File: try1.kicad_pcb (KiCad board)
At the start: 2 copper layers, 175.3 x 119.4 mm, 33 parts, among them J10 Archon-connector-modules-Driv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, J11 Archon-connector-modules-Driv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, J2 Archon-connector-modules-Heat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, J21 DB37, J22 DB37, J3 Archon-connector-modules-Driv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, J31 DB9, J4 Archon-connector-modules-LVBi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, J41 CONN_DVI, J5 Archon-connector-modules-ADC, J6 Archon-connector-modules-ADC, J7 Archon-connector-modules-ADC, J8 Archon-connector-modules-ADC, J9 Archon-connector-modules-HVBi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, P1 CONN_02X02

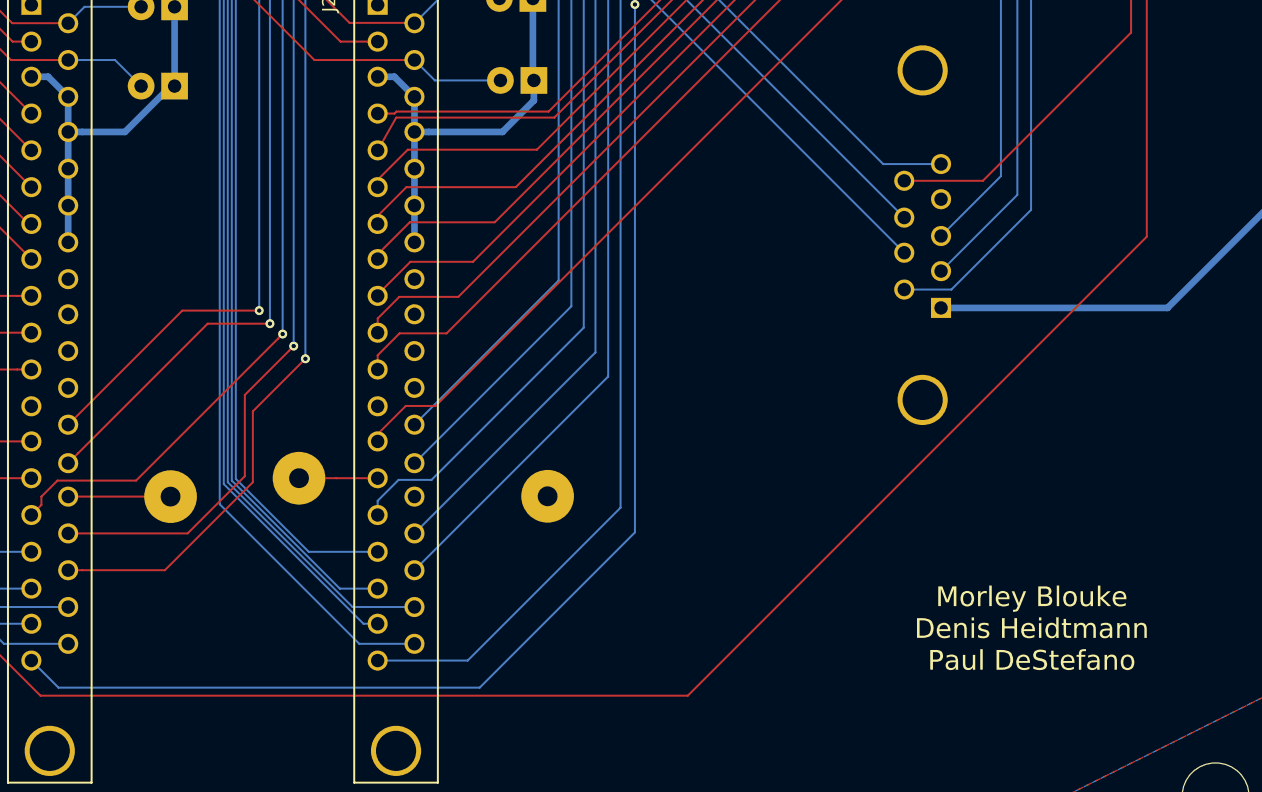
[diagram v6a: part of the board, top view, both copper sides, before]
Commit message: Add Ralf & Erik, Tweak GND Traces
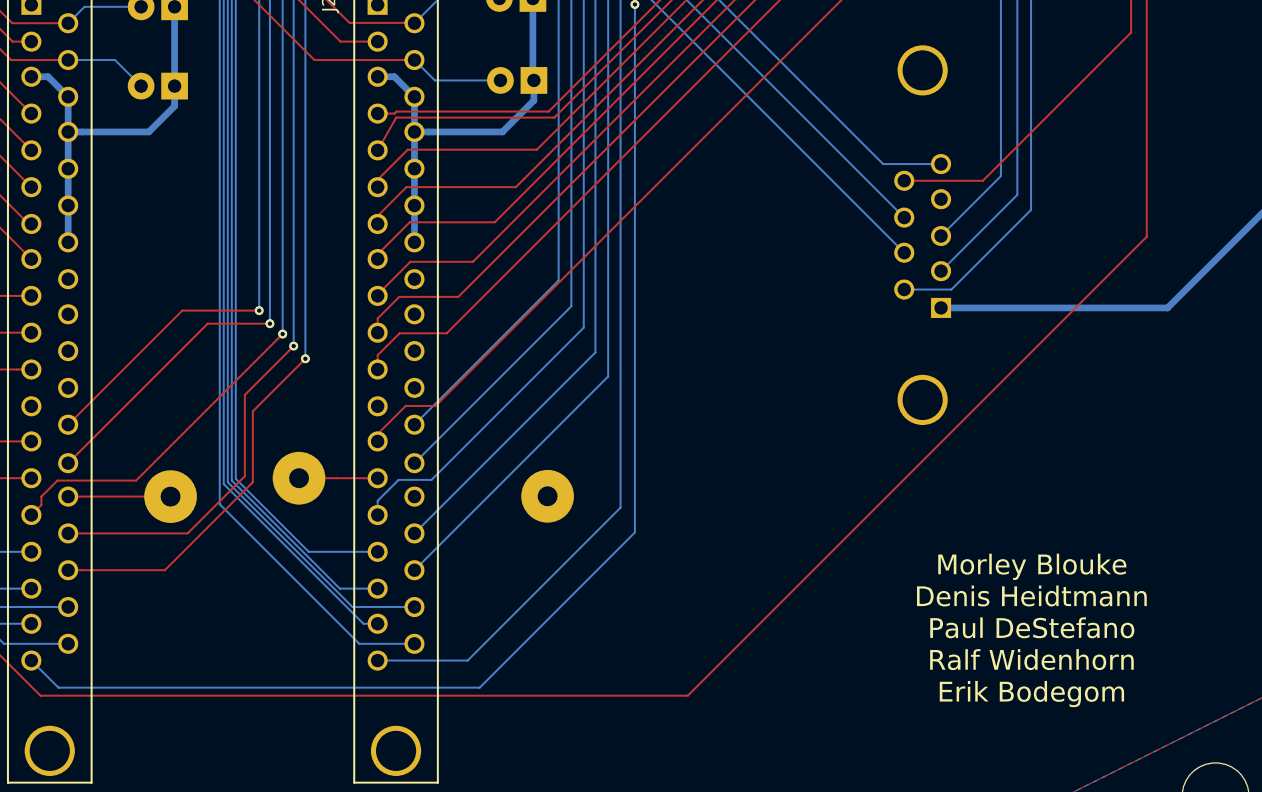
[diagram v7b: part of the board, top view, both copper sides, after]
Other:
- board text added: "Morley Blouke Denis Heidtmann Paul DeStefano Ralf Widenhorn Erik Bodegom"
- board text removed: "Morley Blouke Denis Heidtmann Paul DeStefano"
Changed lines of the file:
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@@
     (pad "" np_thru_hole circle (at -6.6 1.524 90) (size 1.524 1.524) (drill 1.524) (layers *.Cu *.Mask F.SilkS))
   )
-  (gr_text "Morley Blouke\nDenis Heidtmann\nPaul DeStefano" (at 197.6374 122.1486) (layer F.SilkS)
+  (gr_text "Morley Blouke\nDenis Heidtmann\nPaul DeStefano\nRalf Widenhorn\nErik Bodegom" (at 197.6374 122.1486) (layer F.SilkS)
     (effects (font (size 1.5 1.5) (thickness 0.3)))
   )
@@
   (target plus (at 52.07 99.06) (size 5) (width 0.15) (layer Edge.Cuts))
   (target plus (at 52.07 35.56) (size 5) (width 0.15) (layer Edge.Cuts))
+  (segment (start 132.5626 80.9498) (end 132.5626 82.4738) (width 0.508) (layer B.Cu) (net 23))
+  (segment (start 132.5626 82.4738) (end 130.6068 84.4296) (width 0.508) (layer B.Cu) (net 23))
+  (segment (start 130.6068 84.4296) (end 125.56173 84.4296) (width 0.508) (layer B.Cu) (net 23))
+  (segment (start 125.56173 84.4296) (end 124.4841 84.4296) (width 0.508) (layer B.Cu) (net 23))
   (segment (start 150.7744 90.0176) (end 150.7744 92.8116) (width 0.508) (layer B.Cu) (net 23))
   (segment (start 150.7744 87.2236) (end 150.7744 90.0176) (width 0.508) (layer B.Cu) (net 23))
@@
   (segment (start 121.6901 80.2386) (end 122.9601 80.2386) (width 0.508) (layer B.Cu) (net 23))
   (segment (start 122.9601 80.2386) (end 124.4841 81.7626) (width 0.508) (layer B.Cu) (net 23))
-  (segment (start 132.5626 80.9498) (end 132.562599 80.665323) (width 0.508) (layer B.Cu) (net 23))
-  (segment (start 132.562599 80.665323) (end 128.798322 84.4296) (width 0.508) (layer B.Cu) (net 23))
-  (segment (start 128.798322 84.4296) (end 125.56173 84.4296) (width 0.508) (layer B.Cu) (net 23))
-  (segment (start 125.56173 84.4296) (end 124.4841 84.4296) (width 0.508) (layer B.Cu) (net 23))
   (segment (start 124.4841 90.0176) (end 124.4841 92.8116) (width 0.508) (layer B.Cu) (net 23))
   (segment (start 124.4841 90.0176) (end 124.4841 87.2236) (width 0.508) (layer B.Cu) (net 23))

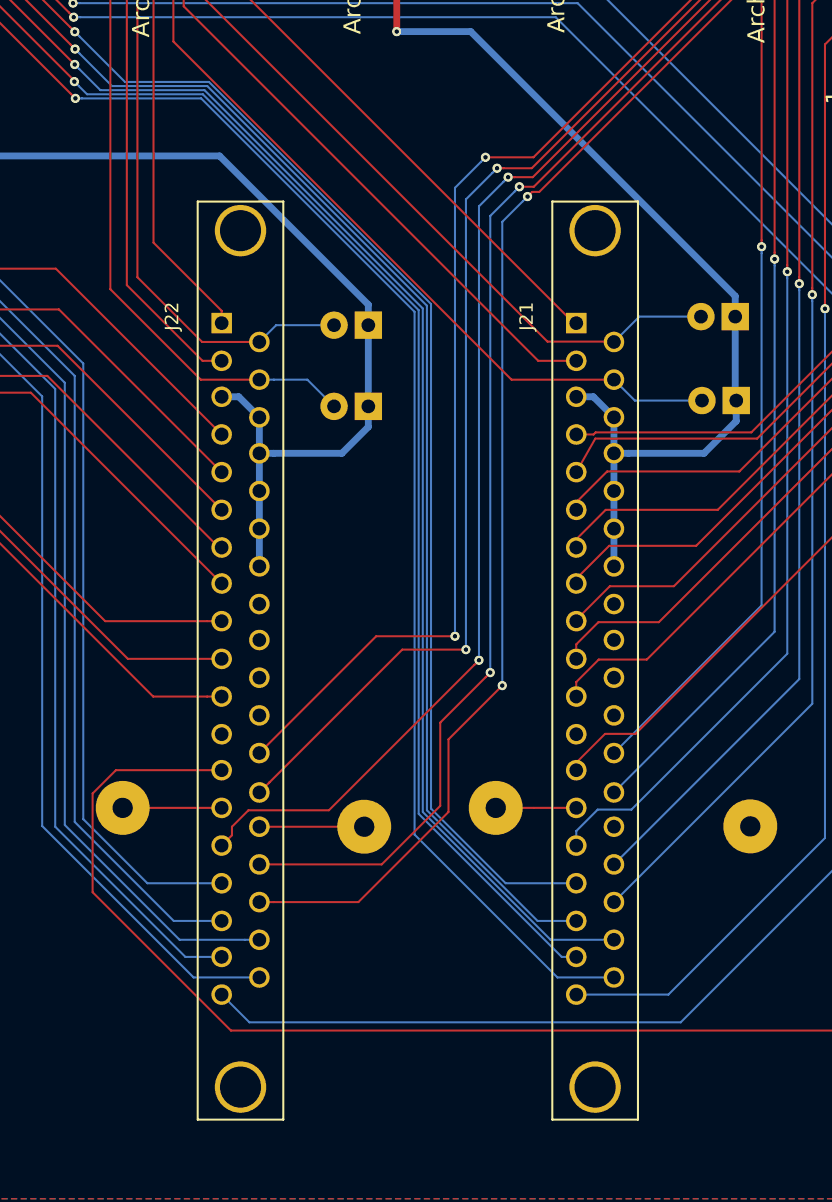
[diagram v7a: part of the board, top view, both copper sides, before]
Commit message: Fix DB37, Need Male Part, Not Female
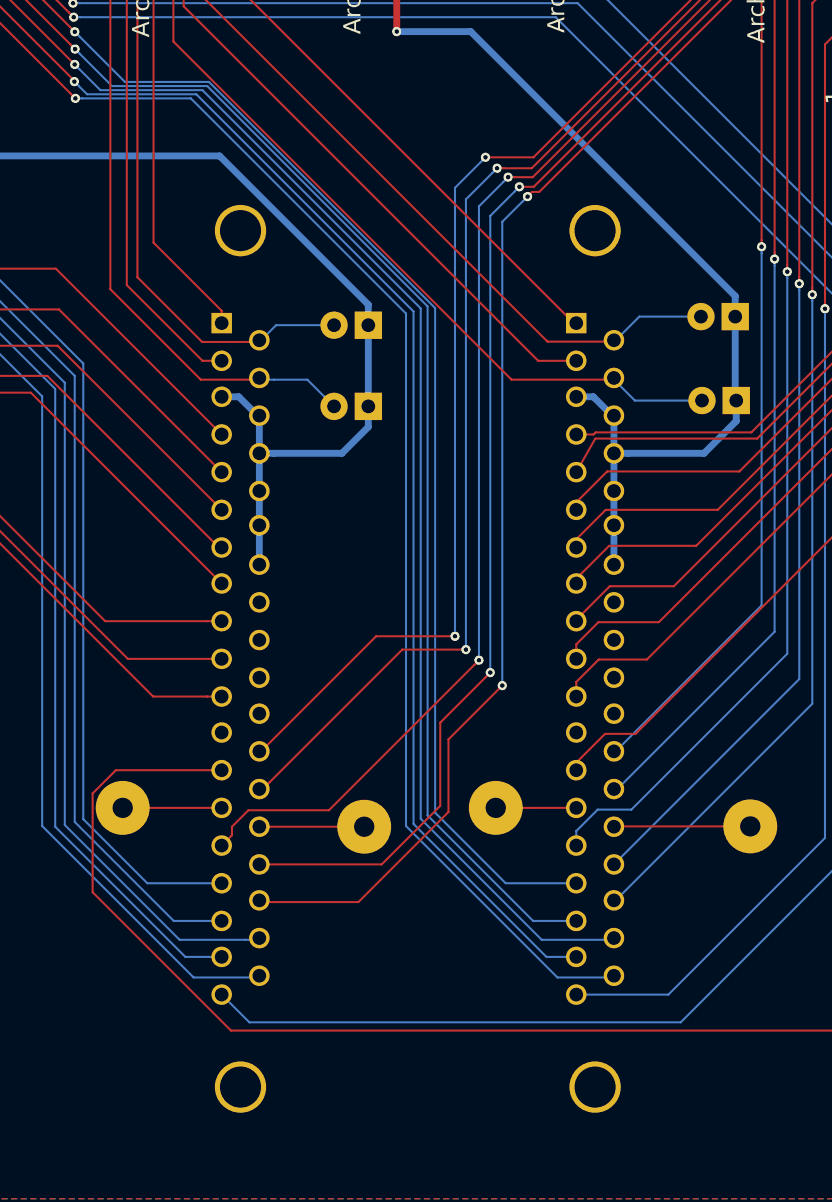
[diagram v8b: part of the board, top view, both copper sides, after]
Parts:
- J21, J22: footprint Connect:DB37FD -> Connect:DB37MD; moved to B.Cu
- turned J21 to 270 degrees
- turned J22 to 270 degrees
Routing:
- net /Spare_4: track 0.00 -> 10.1 mm
